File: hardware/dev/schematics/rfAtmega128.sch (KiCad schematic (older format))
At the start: 59 parts, among them J1 TEST_VDD33, J2 TEST_GND, J3 PWR_ON/OFF, J4 J2PIN, J5 J2PIN, U1 LED_RED, U10 LED_GREEN, U11 LED_GREEN, U12 LED_GREEN, U13 BAT54S, U14 BAT54S, U2 DIODE, U3 Q16.000, U4 BA033CC0WFP, U5 BUTTON, U6 ATMEGA128RFA1, U7 FT232RL, U8 2450FB15L0001, U9 LED_GREEN, X1 RP-SMA

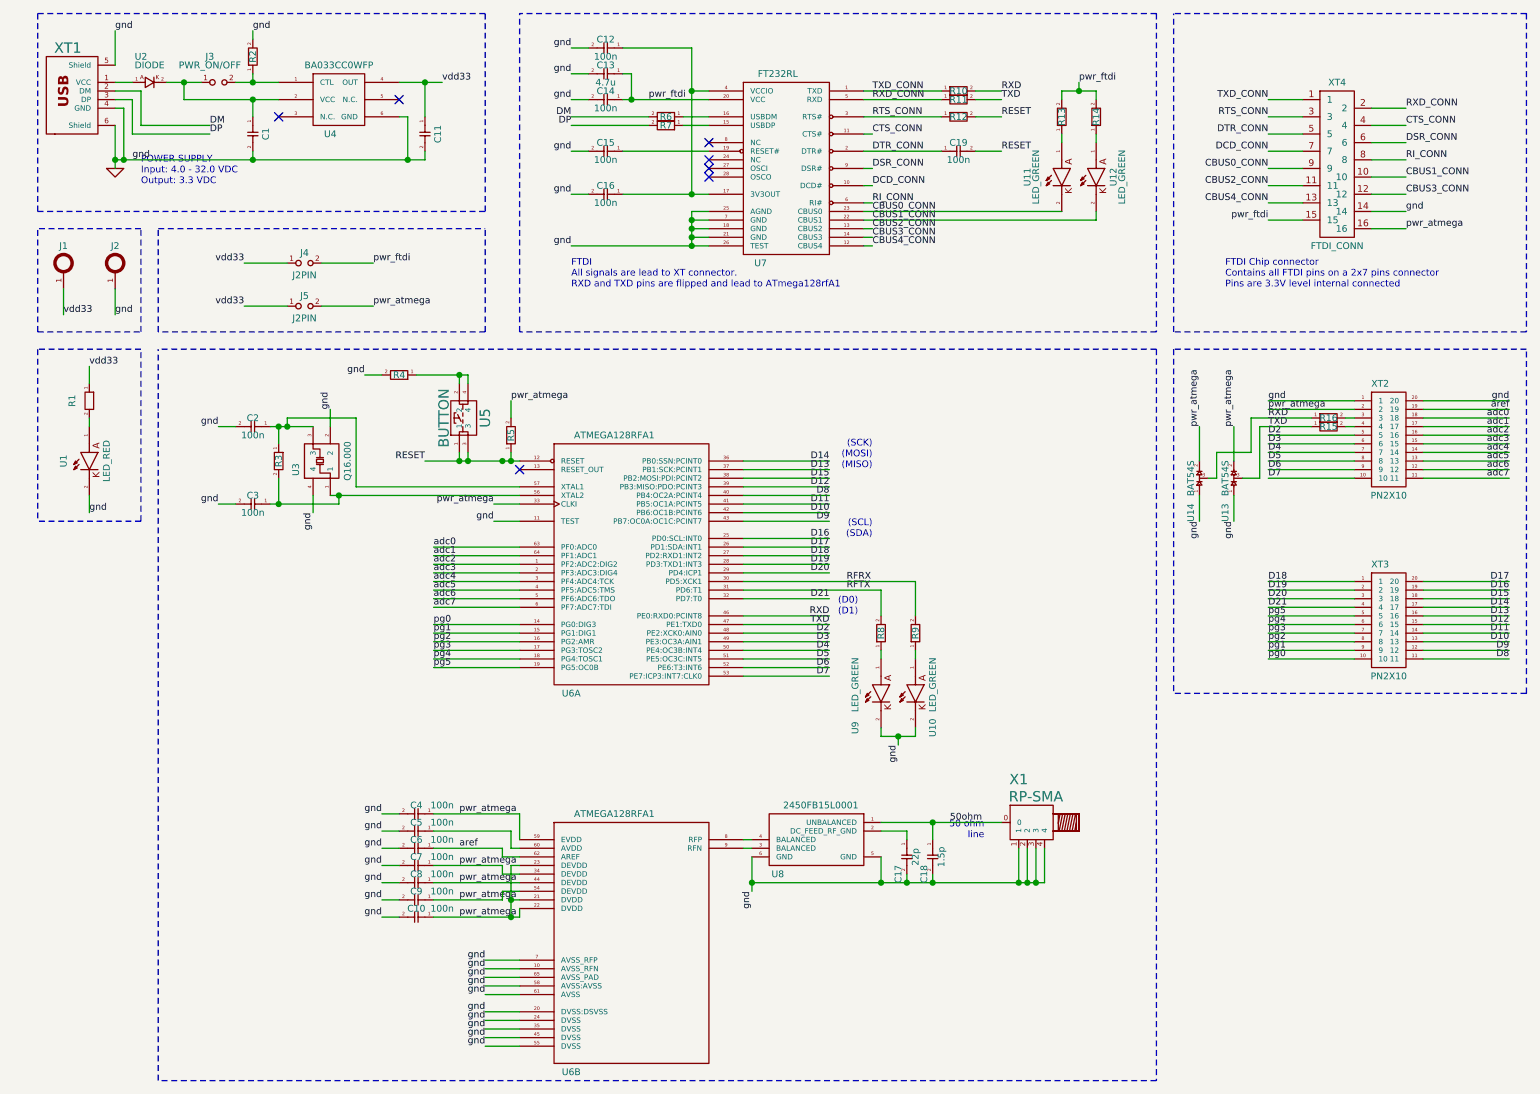
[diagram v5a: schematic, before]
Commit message: Removed test pads, atmega connectors are routed. FTDI connector needs routing.
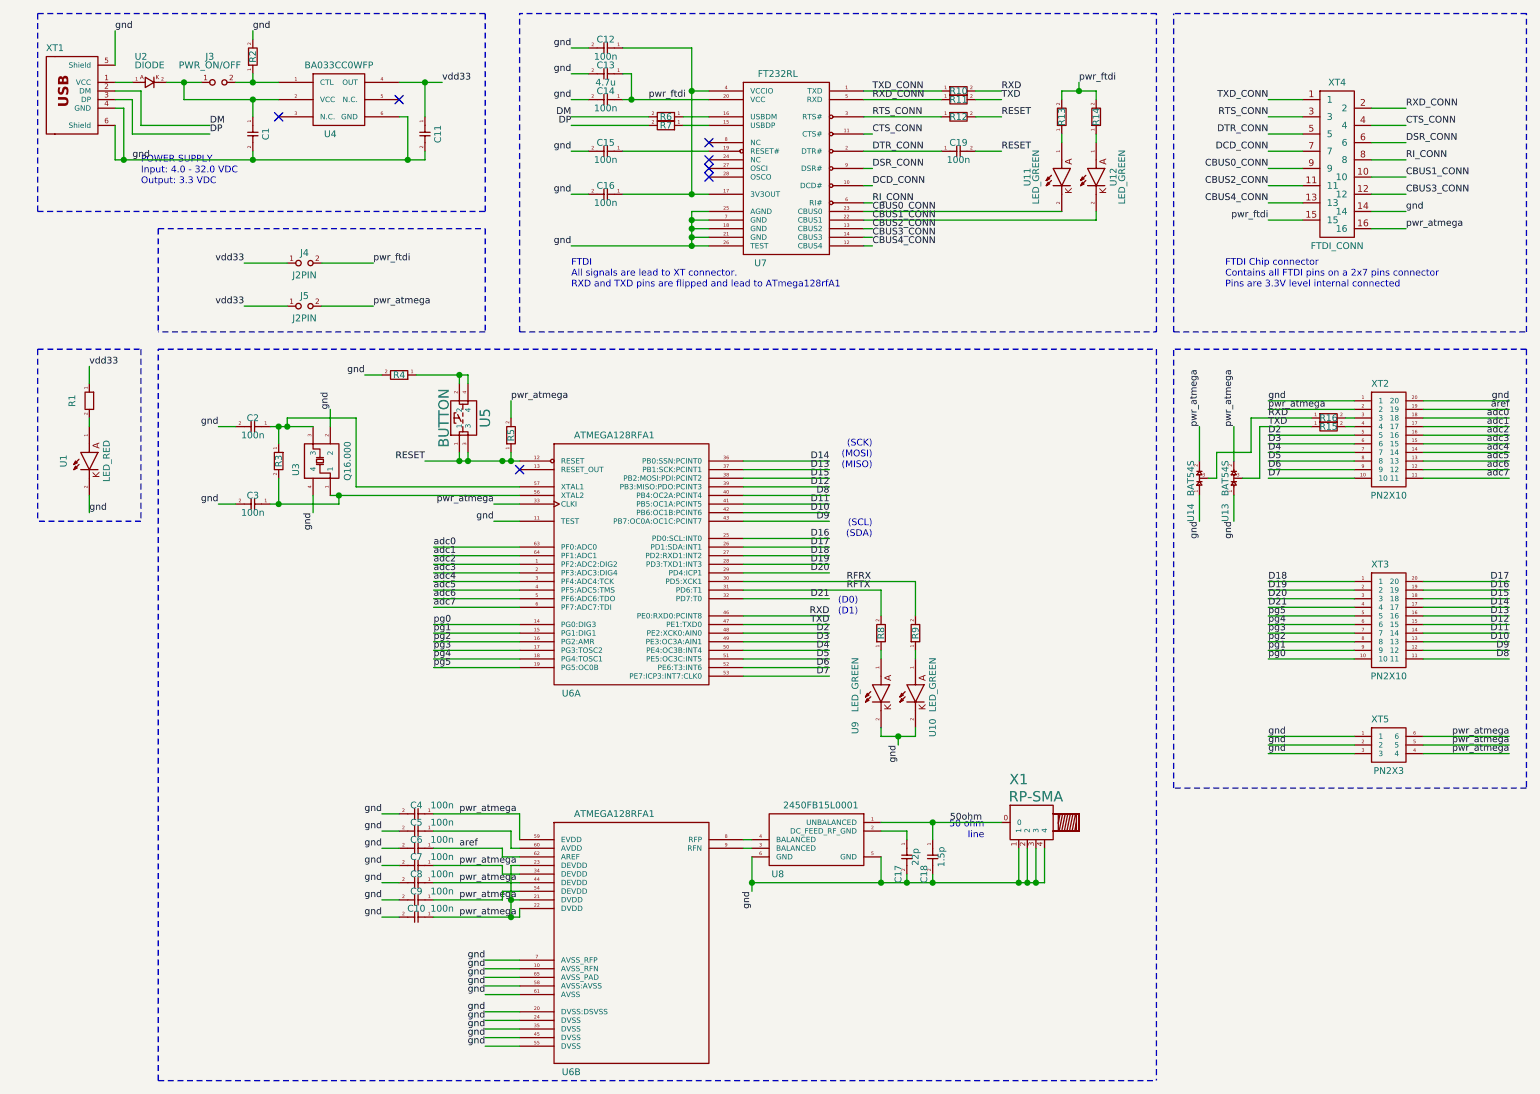
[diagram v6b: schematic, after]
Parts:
- removed J1: TEST_VDD33, testpoint_2mm5, symbol TEST_PAD
- removed J2: TEST_GND, testpoint_2mm5, symbol TEST_PAD
- added XT5: PN2X3, PN2X3, symbol PN2X3
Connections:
- net pwr_atmega: now also XT5.4, XT5.5, XT5.6
- net GND renamed gnd
- net gnd: now also XT5.1, XT5.2, XT5.3
